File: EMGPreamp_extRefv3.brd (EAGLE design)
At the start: 29.5 x 30.8 mm, 25 parts

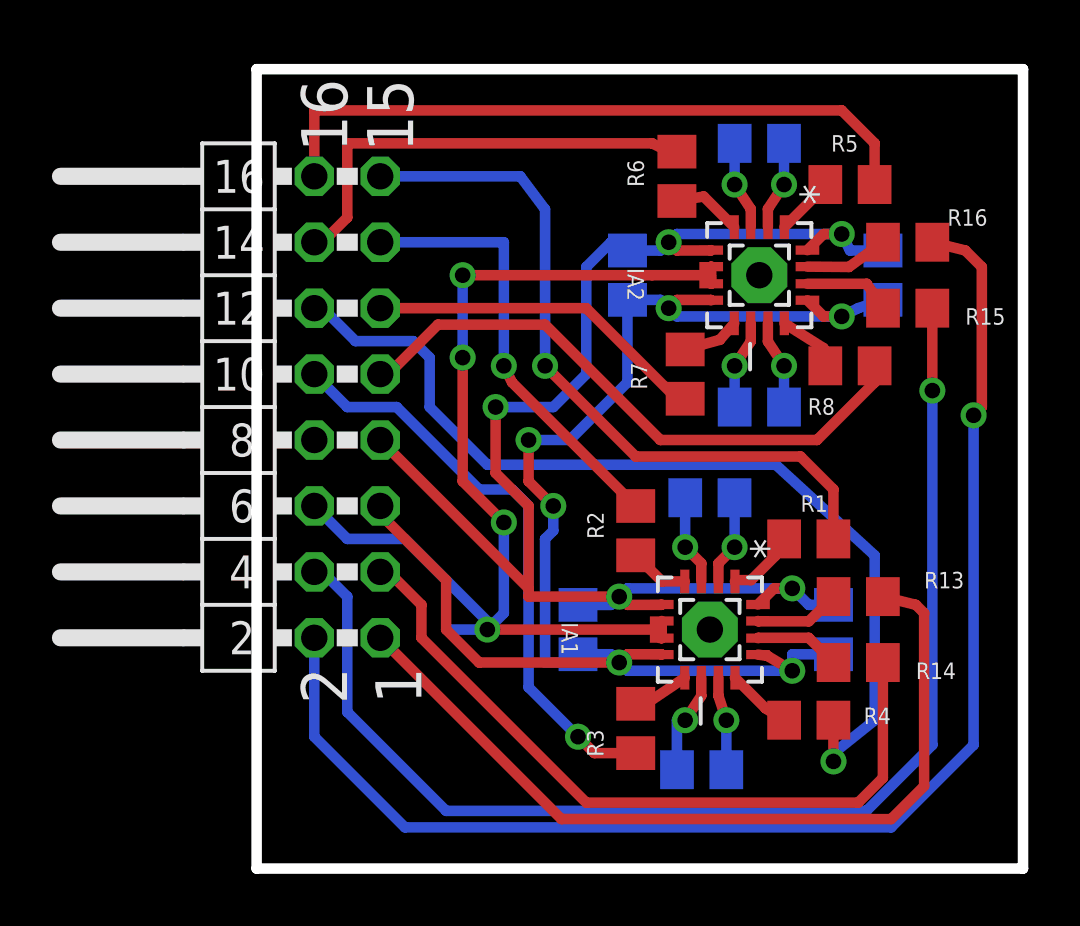
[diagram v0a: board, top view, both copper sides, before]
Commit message: reorganized IO labeling to be consistent on v4 backplane
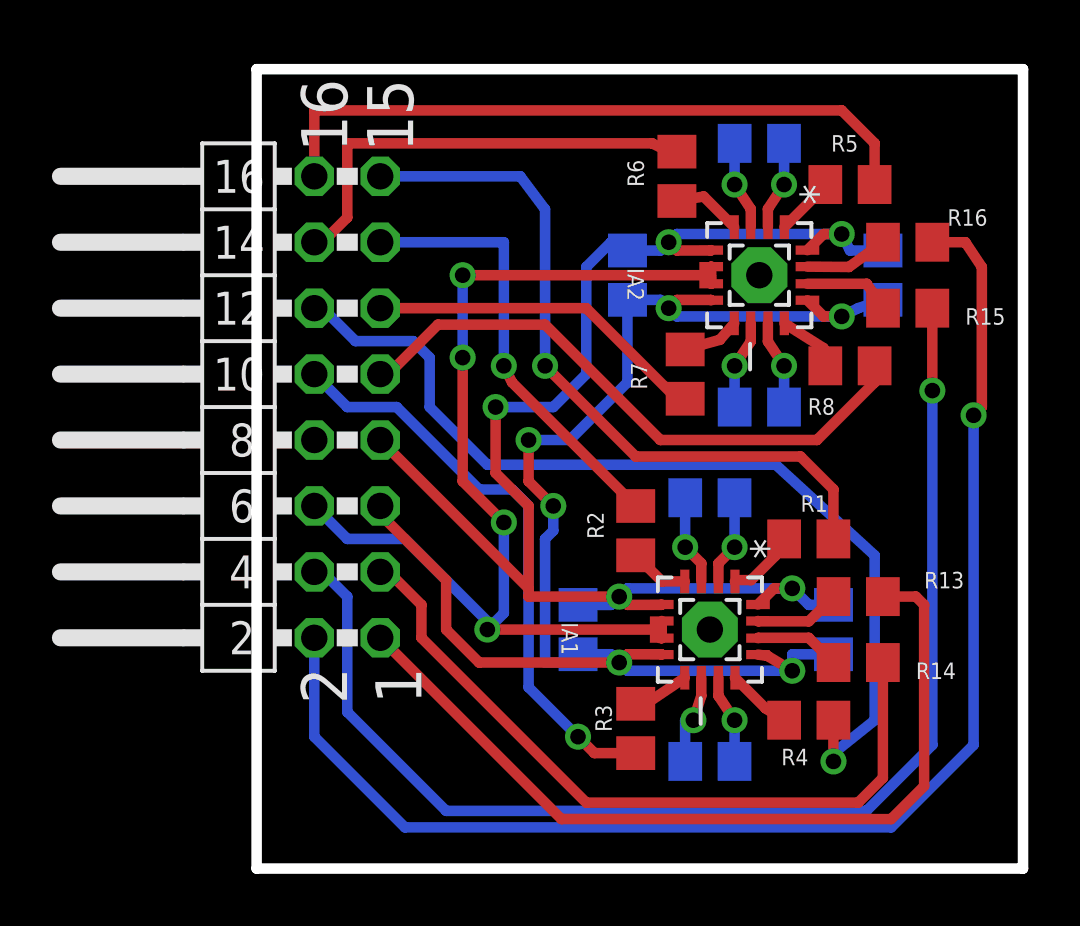
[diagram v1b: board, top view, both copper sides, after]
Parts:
- moved R10 0.45 mm to (16.5, 3.17)
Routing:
- net VREF: track 43.1 -> 41.6 mm
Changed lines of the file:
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@@
 <attribute name="NAME" x="13.335" y="13.6525" size="0.635" layer="26" rot="MR180"/>
 </element>
-<element name="R10" library="rcl" package="R0805" value="499" x="16.1925" y="2.8575" smashed="yes" rot="MR0">
-<attribute name="NAME" x="13.97" y="3.175" size="0.635" layer="26" rot="MR0"/>
+<element name="R10" library="rcl" package="R0805" value="499" x="16.51" y="3.175" smashed="yes" rot="MR0">
+<attribute name="NAME" x="14.2875" y="3.4925" size="0.635" layer="26" rot="MR0"/>
 </element>
 <element name="R11" library="rcl" package="R0805" value="499" x="18.415" y="26.9875" smashed="yes" rot="MR180">
-<attribute name="NAME" x="14.9225" y="27.305" size="0.635" layer="26" rot="MR180"/>
+<attribute name="NAME" x="20.32" y="27.305" size="0.635" layer="26" rot="MR180"/>
 </element>
 <element name="R12" library="rcl" package="R0805" value="499" x="18.415" y="16.8275" smashed="yes" rot="MR0">
@@
 </element>
 <element name="R3" library="rcl" package="R0805" value="20k" x="13.6525" y="4.445" smashed="yes" rot="R90">
-<attribute name="NAME" x="12.4144125" y="3.360990625" size="0.635" layer="25" rot="R90"/>
+<attribute name="NAME" x="12.7319125" y="4.313490625" size="0.635" layer="25" rot="R90"/>
 </element>
 <element name="R4" library="rcl" package="R0805" value="20k" x="20.32" y="4.7625" smashed="yes" rot="R180">
-<attribute name="NAME" x="23.479046875" y="5.2500375" size="0.635" layer="25" rot="R180"/>
+<attribute name="NAME" x="20.304046875" y="3.6625375" size="0.635" layer="25" rot="R180"/>
 </element>
 <element name="R5" library="rcl" package="R0805" value="20k" x="21.9075" y="25.4" smashed="yes" rot="R180">
@@
 <wire x1="14.6558" y1="7.9248" x2="14.5923" y2="7.9248" width="0.4064" layer="1"/>
 <wire x1="16.5481" y1="22.225" x2="16.5608" y2="22.2377" width="0.4064" layer="1"/>
-<wire x1="13.97" y1="21.9075" x2="14.2875" y2="21.9075" width="0.4064" layer="1"/>
-<wire x1="14.2875" y1="21.9075" x2="16.5481" y2="21.9075" width="0.4064" layer="1"/>
 <wire x1="16.5481" y1="21.9075" x2="16.5608" y2="21.5773" width="0.4064" layer="1"/>
 <wire x1="7.9375" y1="8.255" x2="14.3256" y2="8.255" width="0.4064" layer="1"/>
 <wire x1="14.3256" y1="8.255" x2="14.6558" y2="7.9248" width="0.4064" layer="1"/>
 <via x="7.9375" y="8.255" extent="1-16" drill="0.6" shape="square"/>
-<wire x1="7.9375" y1="8.255" x2="6.35" y2="8.255" width="0.4064" layer="16"/>
 <via x="8.5725" y="12.3825" extent="1-16" drill="0.6" shape="square"/>
 <wire x1="8.5725" y1="12.3825" x2="6.985" y2="13.97" width="0.4064" layer="1"/>
@@
 <wire x1="6.985" y1="18.7325" x2="6.985" y2="21.9075" width="0.4064" layer="16"/>
 <via x="6.985" y="21.9075" extent="1-16" drill="0.6" shape="square"/>
-<wire x1="6.985" y1="21.9075" x2="13.97" y2="21.9075" width="0.4064" layer="1"/>
+<wire x1="6.985" y1="21.9075" x2="16.5481" y2="21.9075" width="0.4064" layer="1"/>
 <contactref element="SV1" pad="6"/>
 <wire x1="1.27" y1="13.0175" x2="2.54" y2="11.7475" width="0.4064" layer="16"/>
@@
 <signal name="OUT1">
 <contactref element="R13" pad="2"/>
-<wire x1="23.175" y1="9.525" x2="24.4475" y2="9.2075" width="0.4064" layer="1"/>
-<wire x1="24.4475" y1="9.2075" x2="24.765" y2="8.89" width="0.4064" layer="1"/>
-<wire x1="24.765" y1="8.89" x2="24.765" y2="2.2225" width="0.4064" layer="1"/>
+<wire x1="23.175" y1="9.525" x2="24.4475" y2="9.525" width="0.4064" layer="1"/>
+<wire x1="24.4475" y1="9.525" x2="24.765" y2="9.2075" width="0.4064" layer="1"/>
+<wire x1="24.765" y1="9.2075" x2="24.765" y2="2.2225" width="0.4064" layer="1"/>
 <wire x1="24.765" y1="2.2225" x2="23.495" y2="0.9525" width="0.4064" layer="1"/>
 <wire x1="23.495" y1="0.9525" x2="10.795" y2="0.9525" width="0.4064" layer="1"/>
@@
 <signal name="OUT3">
 <contactref element="R15" pad="2"/>
-<wire x1="25.08" y1="23.1775" x2="26.3525" y2="22.86" width="0.4064" layer="1"/>
-<wire x1="26.3525" y1="22.86" x2="26.9875" y2="22.225" width="0.4064" layer="1"/>
+<wire x1="25.08" y1="23.1775" x2="26.3525" y2="23.1775" width="0.4064" layer="1"/>
+<wire x1="26.3525" y1="23.1775" x2="26.9875" y2="22.225" width="0.4064" layer="1"/>
 <wire x1="26.9875" y1="22.225" x2="26.9875" y2="16.8275" width="0.4064" layer="1"/>
 <wire x1="26.9875" y1="16.8275" x2="26.67" y2="16.51" width="0.4064" layer="1"/>
@@
 <contactref element="R10" pad="1"/>
 <wire x1="16.8402" y1="6.4008" x2="16.8402" y2="5.7023" width="0.4064" layer="1"/>
-<wire x1="16.8402" y1="5.7023" x2="17.145" y2="4.7625" width="0.4064" layer="1"/>
-<via x="17.145" y="4.7625" extent="1-16" drill="0.6" shape="square"/>
-<wire x1="17.145" y1="4.7625" x2="17.145" y2="2.86" width="0.4064" layer="16"/>
-<wire x1="17.145" y1="2.86" x2="17.1425" y2="2.8575" width="0.4064" layer="16"/>
+<wire x1="16.8402" y1="5.7023" x2="17.4625" y2="4.7625" width="0.4064" layer="1"/>
+<via x="17.4625" y="4.7625" extent="1-16" drill="0.6" shape="square"/>
+<wire x1="17.4625" y1="4.7625" x2="17.4625" y2="2.86" width="0.4064" layer="16"/>
+<wire x1="17.4625" y1="2.86" x2="17.46" y2="3.175" width="0.4064" layer="16"/>
 </signal>
 <signal name="RG3">
@@
 <contactref element="R10" pad="2"/>
 <wire x1="16.1798" y1="6.4008" x2="16.1798" y2="5.7023" width="0.4064" layer="1"/>
-<wire x1="16.1798" y1="5.7023" x2="15.5575" y2="4.7625" width="0.4064" layer="1"/>
-<via x="15.5575" y="4.7625" extent="1-16" drill="0.6" shape="square"/>
-<wire x1="15.5575" y1="4.7625" x2="15.24" y2="4.7625" width="0.4064" layer="16"/>
-<wire x1="15.24" y1="4.7625" x2="15.24" y2="2.86" width="0.4064" layer="16"/>
-<wire x1="15.24" y1="2.86" x2="15.2425" y2="2.8575" width="0.4064" layer="16"/>
+<wire x1="16.1798" y1="5.7023" x2="15.875" y2="4.7625" width="0.4064" layer="1"/>
+<via x="15.875" y="4.7625" extent="1-16" drill="0.6" shape="square"/>
+<wire x1="15.875" y1="4.7625" x2="15.5575" y2="4.7625" width="0.4064" layer="16"/>
+<wire x1="15.5575" y1="4.7625" x2="15.5575" y2="2.86" width="0.4064" layer="16"/>
+<wire x1="15.5575" y1="2.86" x2="15.56" y2="3.175" width="0.4064" layer="16"/>
 </signal>
 <signal name="RG3_2">
